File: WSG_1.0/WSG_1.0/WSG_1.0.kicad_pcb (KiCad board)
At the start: 4 copper layers, 68.8 x 27.7 mm, 123 parts, among them J1 Conn_01x10, J2 USB_C_Receptacle_USB2.0_16P, J4 Conn_01x02, SW3 SW_Push, SW4 SW_Push, U1 ADS131A04IPBSR, U10 TPS22916CYFPR, U11 W25N04KVZEIR, U12 USBLC6-2SC6, U14 TPD4E1U06DBVR, U15 ESP32-S3-MINI-1U-N8, U2 DAC60501ZDGSR, U3 INA827AIDGKR, U4 INA827AIDGKR, U5 INA827AIDGKR, U6 TMP235A2DBZR, U7 BQ25180YBGR, U8 TPS63802DLAR, U9 TPS7A2025PDBVR, Y1 SiT8008AI-12-33S-16.384000

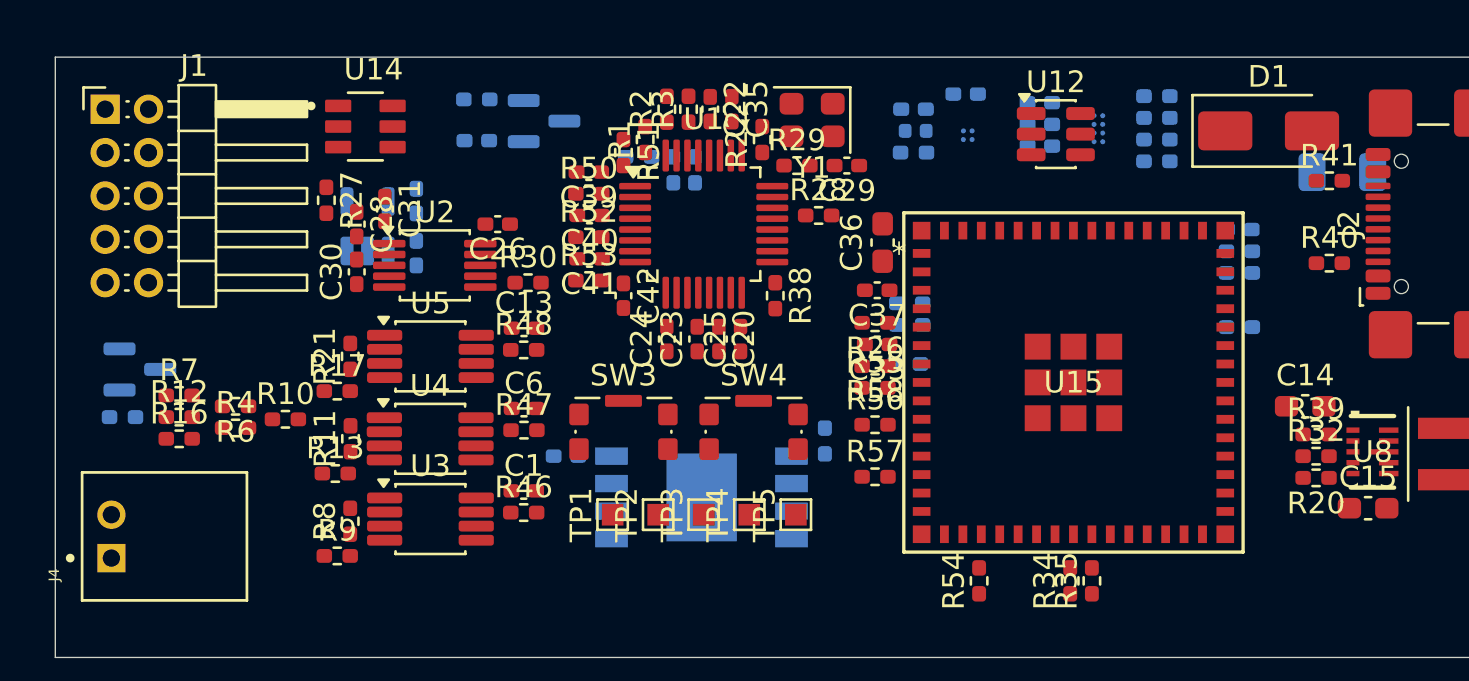
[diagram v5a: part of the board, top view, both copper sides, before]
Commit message: ground pour
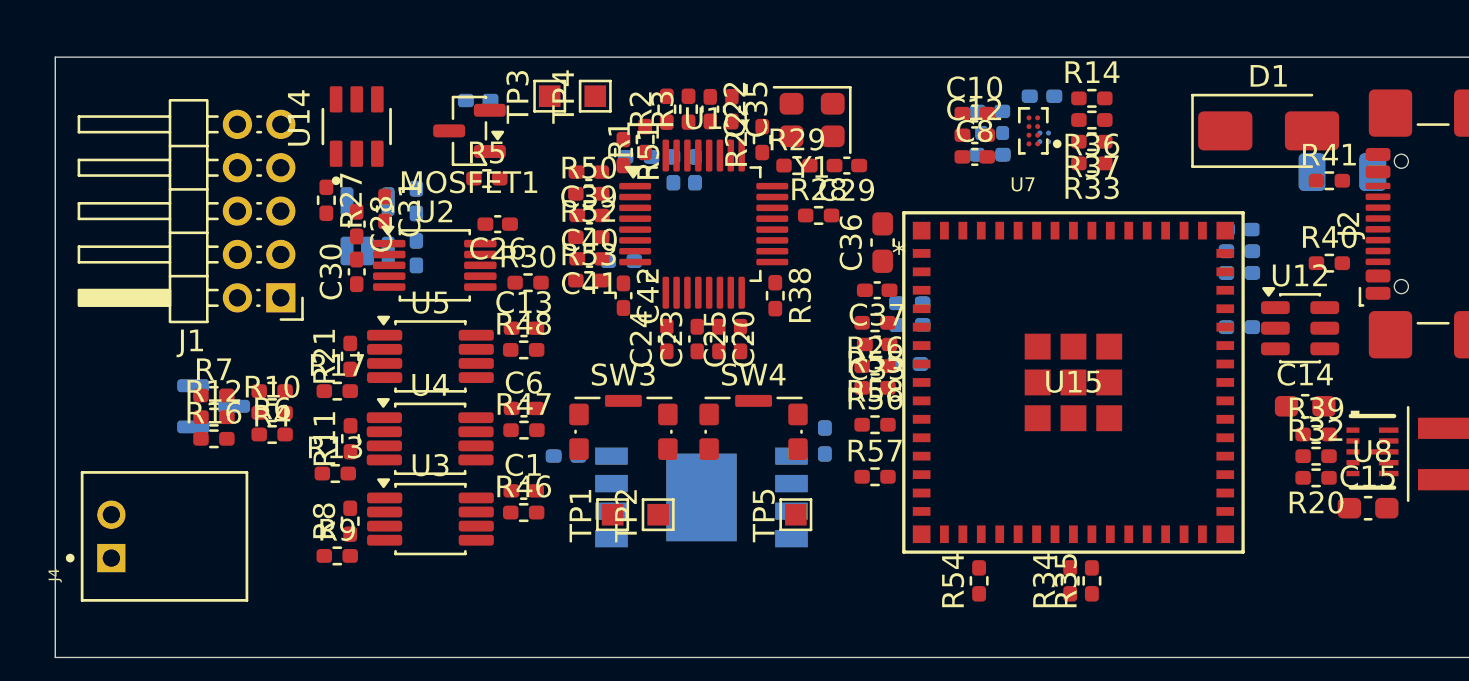
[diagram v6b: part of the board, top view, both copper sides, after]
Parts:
- C10, C12, C8, MOSFET1, R14, R33, R36, R37, R5, U7: moved to F.Cu
- moved TP3 20.6 mm to (109.1, 63.2)
- moved TP4 20.6 mm to (111.2, 63.2)
- moved U6 20.1 mm to (93.6, 77.5)
- moved R5 20.1 mm to (106.2, 67.0), turned to 0 degrees
- moved MOSFET1 18.8 mm to (105.4, 64.8), turned to 180 degrees
- moved U12 14.4 mm to (143.7, 73.9)
- moved J1 11.9 mm to (96.7, 72.5), turned to 180 degrees
- moved R49 9.99 mm to (112.4, 70.8), turned to 0 degrees
- moved R33 4.31 mm to (134.1, 66.3)
- moved R14 4.17 mm to (134.1, 63.3)
- moved C8 3.91 mm to (128.7, 66.0)
- moved C2 3.53 mm to (131.8, 63.2)
- moved C34 3.53 mm to (129.4, 63.9)
- moved FB1 3.53 mm to (129.5, 64.9)
- moved R24 3.53 mm to (129.4, 65.9)
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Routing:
- added copper zone on In1.Cu, net GND

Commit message: ~1/2 done with routing, neeed to undo some
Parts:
- R49: moved to F.Cu
- moved C2 29.3 mm to (102.5, 62.8)
- moved C34 24.3 mm to (105.1, 64.9)
- moved R24 24.3 mm to (105.1, 66.9)
- moved U10 24.3 mm to (107.6, 66.1)
- moved FB1 24.3 mm to (105.2, 65.9)
- moved C21 21.5 mm to (90.5, 78.5)
- moved C20 18.6 mm to (98.8, 70.3)
- moved R49 2.55 mm to (113.5, 73.1), turned to 90 degrees
- moved C38 1.50 mm to (142.4, 69.4)
- moved R43 1.50 mm to (142.4, 73.9)
- moved R45 1.50 mm to (142.4, 70.4)
- moved R44 1.50 mm to (142.4, 71.3)
- moved R15 1.31 mm to (115.1, 67.7)
- moved R18 1.31 mm to (114.1, 67.7)
- moved C22 1.10 mm to (116.5, 62.7)
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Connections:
- C20 pad 1: REFEXT_F -> Net-(C20-Pad1)
- R27 pad 2: REFEXT_F -> Net-(C20-Pad1)
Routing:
- net GND: track 0.00 -> 42.1 mm, vias 0 -> 40
- net BATT_P: track 0.00 -> 37.6 mm
- net VREF_1V65: track 0.00 -> 22.8 mm, vias 0 -> 1
- net 3V3A: track 0.00 -> 21.7 mm, vias 0 -> 3
- net ADC_SCLK: track 0.00 -> 20.8 mm, vias 0 -> 2
- net BREF_F: track 0.00 -> 19.2 mm
- net ADC_MOSI: track 0.00 -> 17.2 mm, vias 0 -> 2
- net EXC_2V5: track 0.00 -> 17.0 mm, vias 0 -> 2
- net VBAT: track 0.00 -> 15.8 mm, vias 0 -> 1
- net BATT_N: track 0.00 -> 15.3 mm
- net 3V3: track 0.00 -> 8.11 mm, vias 0 -> 1
- net SIG1: track 0.00 -> 6.53 mm
- net SIG2: track 0.00 -> 5.90 mm
- net VBUS: track 0.00 -> 4.31 mm, vias 0 -> 1
- net SYS: track 0.00 -> 4.02 mm, vias 0 -> 3
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- added copper zone on In2.Cu, net 3V3
- added copper zone on In2.Cu, net 3V3A
- added copper zone on In2.Cu, net SYS
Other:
- board size 68.8 x 27.7 mm -> 68.8 x 28.3 mm

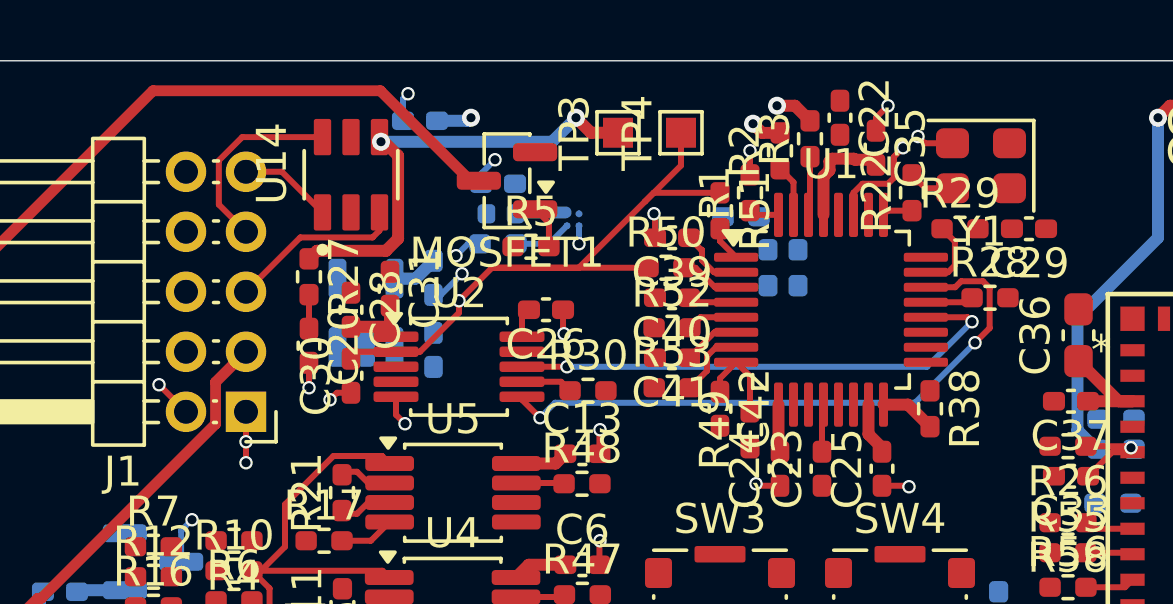
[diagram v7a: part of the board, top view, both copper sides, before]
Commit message: adjuts placement slightly, reroute
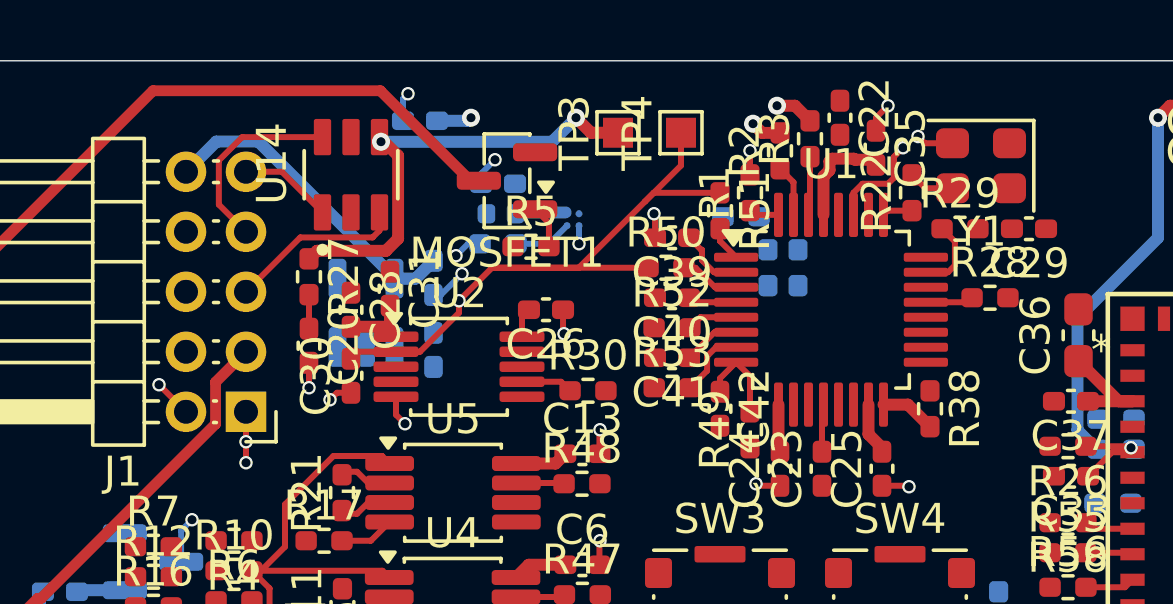
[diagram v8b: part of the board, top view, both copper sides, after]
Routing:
- net ADC_SCLK: track 20.8 -> 0.00 mm, vias 2 -> 0
- net ADC_MOSI: track 17.2 -> 0.00 mm, vias 2 -> 0
- net EXC_2V5: track 17.0 -> 26.3 mm
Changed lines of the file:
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@@
+	)
+	(segment
+		(start 101.65 68.028715)
+		(end 97.116285 63.495)
+		(width 0.4)
+		(layer "B.Cu")
+		(net "EXC_2V5")
+	)
+	(segment
+		(start 97.116285 63.495)
+		(end 95.705 63.495)
+		(width 0.4)
+		(layer "B.Cu")
+		(net "EXC_2V5")
+	)
+	(segment
+		(start 95.705 63.495)
+		(end 94.7 64.5)
+		(width 0.4)
+		(layer "B.Cu")
+		(net "EXC_2V5")
 	)
 	(segment
@@
 		(start 107.7 62.7)
 		(end 106.9 63.5)
+		(width 0.4)
+		(layer "B.Cu")
+		(net "EXC_2V5")
+	)
+	(segment
+		(start 101.65 68.0625)
+		(end 101.65 68.028715)
 		(width 0.4)
 		(layer "B.Cu")
@@
 		(layer "F.Cu")
 		(net "SIG0")
-	)
-	(segment
-		(start 105.9 72)
-		(end 105.9 72.1)
-		(width 0.2)
-		(layer "F.Cu")
-		(net "ADC_SCLK")
-	)
-	(segment
-		(start 121.49 69.71)
-		(end 121.49 68.374022)
-		(width 0.2)
-		(layer "F.Cu")
-		(net "ADC_SCLK")
-	)
-	(segment
-		(start 120.539022 68.15)
-		(end 120.339022 68.35)
-		(width 0.2)
-		(layer "F.Cu")
-		(net "ADC_SCLK")
-	)
-	(segment
-		(start 121 70.2)
-		(end 121.49 69.71)
-		(width 0.2)
-		(layer "F.Cu")
-		(net "ADC_SCLK")
-	)
-	(segment
-		(start 105.9 72.1)
-		(end 106.5 72.7)
-		(width 0.2)
-		(layer "F.Cu")
-		(net "ADC_SCLK")
-	)
-	(segment
-		(start 121.265978 68.15)
-		(end 120.539022 68.15)
-		(width 0.2)
-		(layer "F.Cu")
-		(net "ADC_SCLK")
-	)
-	(segment
-		(start 121.49 68.374022)
-		(end 121.265978 68.15)
-		(width 0.2)
-		(layer "F.Cu")
-		(net "ADC_SCLK")
-	)
-	(segment
-		(start 120.339022 68.35)
-		(end 119.3625 68.35)
-		(width 0.2)
-		(layer "F.Cu")
-		(net "ADC_SCLK")
-	)
-	(via
-		(at 121 70.2)
-		(size 0.45)
-		(drill 0.3)
-		(layers "F.Cu" "B.Cu")
-		(net "ADC_SCLK")
-	)
-	(via
-		(at 106.5 72.7)
-		(size 0.45)
-		(drill 0.3)
-		(layers "F.Cu" "B.Cu")
-		(net "ADC_SCLK")
-	)
-	(segment
-		(start 107 72.2)
-		(end 119 72.2)
-		(width 0.2)
-		(layer "B.Cu")
-		(net "ADC_SCLK")
-	)
-	(segment
-		(start 119 72.2)
-		(end 121 70.2)
-		(width 0.2)
-		(layer "B.Cu")
-		(net "ADC_SCLK")
-	)
-	(segment
-		(start 106.5 72.7)
-		(end 107 72.2)
-		(width 0.2)
-		(layer "B.Cu")
-		(net "ADC_SCLK")
 	)
 	(segment
@@
 	)
 	(segment
-		(start 120.75 69.35)
-		(end 119.3625 69.35)
-		(width 0.2)
-		(layer "F.Cu")
-		(net "ADC_MOSI")
-	)
-	(segment
-		(start 120.9 69.5)
-		(end 120.75 69.35)
-		(width 0.2)
-		(layer "F.Cu")
-		(net "ADC_MOSI")
-	)
-	(segment
-		(start 105.9 71)
-		(end 107.4 71)
-		(width 0.2)
-		(layer "F.Cu")
-		(net "ADC_MOSI")
-	)
-	(via
-		(at 120.9 69.5)
-		(size 0.45)
-		(drill 0.3)
-		(layers "F.Cu" "B.Cu")
-		(net "ADC_MOSI")
-	)
-	(via
-		(at 107.4 71)
-		(size 0.45)
-		(drill 0.3)
-		(layers "F.Cu" "B.Cu")
-		(net "ADC_MOSI")
-	)
-	(segment
-		(start 107.4 71)
-		(end 119.4 71)
-		(width 0.2)
-		(layer "B.Cu")
-		(net "ADC_MOSI")
-	)
-	(segment
-		(start 119.4 71)
-		(end 120.9 69.5)
-		(width 0.2)
-		(layer "B.Cu")
-		(net "ADC_MOSI")
-	)
-	(segment
